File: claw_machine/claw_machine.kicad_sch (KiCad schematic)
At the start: 21 parts, among them J101 Conn_01x04, J102 Conn_01x04, J103 Conn_01x04, J12V_1 Screw_Terminal_01x02, J12V_2 Screw_Terminal_01x02, J5V_1 Screw_Terminal_01x02, J5V_2 Screw_Terminal_01x02, SW4 SW_Push

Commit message: Tiny bit of PCB work
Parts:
- added C101, C102: 100u, Capacitor_THT:CP_Radial_D10.0mm_P5.00mm_P7.50mm, symbol Device:C_Polarized
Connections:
- net +12V: now also C101.1
- net +5V: now also C102.1
- net GND: now also C101.2, C102.2
- no-connect marks 27 -> 33
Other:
- note added: "Motor Bypass Caps"
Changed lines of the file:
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@@
   (no_connect (at 43.18 121.92))
   (no_connect (at 43.18 86.36))
+  (no_connect (at 43.18 35.56))
   (no_connect (at 43.18 83.82))
+  (no_connect (at 43.18 43.18))
   (no_connect (at 80.01 13.97))
   (no_connect (at 77.47 13.97))
   (no_connect (at 109.22 48.26))
+  (no_connect (at 43.18 40.64))
   (no_connect (at 109.22 45.72))
+  (no_connect (at 43.18 38.1))
   (no_connect (at 109.22 132.08))
   (no_connect (at 43.18 76.2))
+  (no_connect (at 43.18 48.26))
   (no_connect (at 43.18 81.28))
   (no_connect (at 109.22 129.54))
@@
   (no_connect (at 43.18 99.06))
   (no_connect (at 109.22 134.62))
+  (no_connect (at 43.18 45.72))
   (no_connect (at 43.18 78.74))
   (no_connect (at 43.18 96.52))
@@
   (no_connect (at 43.18 91.44))
   (no_connect (at 74.93 13.97))
+  (wire (pts (xy 173.99 121.92) (xy 173.99 123.19))
+    (stroke (width 0) (type default))
+  )
   (wire (pts (xy 109.22 109.22) (xy 124.46 109.22))
     (stroke (width 0) (type default))
@@
     (stroke (width 0) (type default))
   )
+  (wire (pts (xy 186.69 121.92) (xy 186.69 123.19))
+    (stroke (width 0) (type default))
+  )
   (wire (pts (xy 39.37 104.14) (xy 43.18 104.14))
     (stroke (width 0) (type default))
   )
+  (wire (pts (xy 173.99 113.03) (xy 173.99 114.3))
+    (stroke (width 0) (type default))
+  )
   (wire (pts (xy 109.22 68.58) (xy 118.11 68.58))
     (stroke (width 0) (type default))
@@
     (stroke (width 0) (type default))
   )
+  (wire (pts (xy 186.69 113.03) (xy 186.69 114.3))
+    (stroke (width 0) (type default))
+  )
   (wire (pts (xy 26.67 193.04) (xy 26.67 191.77))
     (stroke (width 0) (type default))
@@
   )
   (rectangle (start 48.26 154.94) (end 101.6 200.66)
+    (stroke (width 0) (type default))
+    (fill (type none))
+  )
+  (rectangle (start 160.02 106.68) (end 215.9 129.54)
     (stroke (width 0) (type default))
     (fill (type none))
@@
   )
   (text "Stepper Drivers" (at 229.87 109.22 0)
+    (effects (font (size 1.27 1.27) (thickness 0.254) bold) (justify left bottom))
+  )
+  (text "Motor Bypass Caps" (at 195.58 110.49 0)
     (effects (font (size 1.27 1.27) (thickness 0.254) bold) (justify left bottom))
   )
@@
     )
   )
+  (symbol (lib_id "power:+12V") (at 173.99 113.03 0) (unit 1)
+    (in_bom yes) (on_board yes) (dnp no)
+    (property "Reference" "#PWR0121" (at 173.99 116.84 0)
+      (effects (font (size 1.27 1.27)) hide)
+    )
+    (property "Value" "+12V" (at 170.18 109.22 0)
+      (effects (font (size 1.27 1.27)) (justify left))
+    )
+    (property "Footprint" "" (at 173.99 113.03 0)
+      (effects (font (size 1.27 1.27)) hide)
+    )
+    (property "Datasheet" "" (at 173.99 113.03 0)
+      (effects (font (size 1.27 1.27)) hide)
+    )
+    (pin "1")
+    (instances
+      (project "claw_machine"
+        (path "/2e48e9a4-e55f-4bd7-8086-6a8b9c5eabc1"
+          (reference "#PWR0121") (unit 1)
+        )
+      )
+      (project "ClawMachine"
+        (path "/aafe1d38-cfbd-4a85-a256-fbe14cd8b9f5"
+          (reference "#PWR046") (unit 1)
+        )
+      )
+    )
+  )
   (symbol (lib_id "Mechanical:MountingHole") (at 172.72 168.91 0) (unit 1)
     (in_bom yes) (on_board yes) (dnp no) (fields_autoplaced)
@@
     )
   )
+  (symbol (lib_id "power:GND") (at 173.99 123.19 0) (unit 1)
+    (in_bom yes) (on_board yes) (dnp no)
+    (property "Reference" "#PWR0122" (at 173.99 129.54 0)
+      (effects (font (size 1.27 1.27)) hide)
+    )
+    (property "Value" "GND" (at 173.99 127 0)
+      (effects (font (size 1.27 1.27)))
+    )
+    (property "Footprint" "" (at 173.99 123.19 0)
+      (effects (font (size 1.27 1.27)) hide)
+    )
+    (property "Datasheet" "" (at 173.99 123.19 0)
+      (effects (font (size 1.27 1.27)) hide)
+    )
+    (pin "1")
+    (instances
+      (project "claw_machine"
+        (path "/2e48e9a4-e55f-4bd7-8086-6a8b9c5eabc1"
+          (reference "#PWR0122") (unit 1)
+        )
+      )
+    )
+  )
   (symbol (lib_id "Switch:SW_Push") (at 34.29 104.14 0) (unit 1)
     (in_bom yes) (on_board yes) (dnp no)
@@
     )
   )
+  (symbol (lib_id "power:GND") (at 186.69 123.19 0) (unit 1)
+    (in_bom yes) (on_board yes) (dnp no)
+    (property "Reference" "#PWR0125" (at 186.69 129.54 0)
+      (effects (font (size 1.27 1.27)) hide)
+    )
+    (property "Value" "GND" (at 186.69 127 0)
+      (effects (font (size 1.27 1.27)))
+    )
+    (property "Footprint" "" (at 186.69 123.19 0)
+      (effects (font (size 1.27 1.27)) hide)
+    )
+    (property "Datasheet" "" (at 186.69 123.19 0)
+      (effects (font (size 1.27 1.27)) hide)
+    )
+    (pin "1")
+    (instances
+      (project "claw_machine"
+        (path "/2e48e9a4-e55f-4bd7-8086-6a8b9c5eabc1"
+          (reference "#PWR0125") (unit 1)
+        )
+      )
+    )
+  )
   (symbol (lib_id "power:+5V") (at 201.93 158.75 0) (unit 1)
     (in_bom yes) (on_board yes) (dnp no)
@@
     )
   )
+  (symbol (lib_id "Device:C_Polarized") (at 186.69 118.11 0) (unit 1)
+    (in_bom yes) (on_board yes) (dnp no) (fields_autoplaced)
+    (property "Reference" "C102" (at 190.5 115.951 0)
+      (effects (font (size 1.27 1.27)) (justify left))
+    )
+    (property "Value" "100u" (at 190.5 118.491 0)
+      (effects (font (size 1.27 1.27)) (justify left))
+    )
+    (property "Footprint" "Capacitor_THT:CP_Radial_D10.0mm_P5.00mm_P7.50mm" (at 187.6552 121.92 0)
+      (effects (font (size 1.27 1.27)) hide)
+    )
+    (property "Datasheet" "~" (at 186.69 118.11 0)
+      (effects (font (size 1.27 1.27)) hide)
+    )
+    (pin "1")
+    (pin "2")
+    (instances
+      (project "claw_machine"
+        (path "/2e48e9a4-e55f-4bd7-8086-6a8b9c5eabc1"
+          (reference "C102") (unit 1)
+        )
+      )
+    )
+  )
   (symbol (lib_id "Device:LED") (at 69.85 180.34 90) (unit 1)
     (in_bom yes) (on_board yes) (dnp no)
@@
         (path "/aafe1d38-cfbd-4a85-a256-fbe14cd8b9f5"
           (reference "#PWR047") (unit 1)
+        )
+      )
+    )
+  )
+  (symbol (lib_id "power:+5V") (at 186.69 113.03 0) (unit 1)
+    (in_bom yes) (on_board yes) (dnp no)
+    (property "Reference" "#PWR0123" (at 186.69 116.84 0)
+      (effects (font (size 1.27 1.27)) hide)
+    )
+    (property "Value" "+5V" (at 186.69 109.22 0)
+      (effects (font (size 1.27 1.27)))
+    )
+    (property "Footprint" "" (at 186.69 113.03 0)
+      (effects (font (size 1.27 1.27)) hide)
+    )
+    (property "Datasheet" "" (at 186.69 113.03 0)
+      (effects (font (size 1.27 1.27)) hide)
+    )
+    (pin "1")
+    (instances
+      (project "claw_machine"
+        (path "/2e48e9a4-e55f-4bd7-8086-6a8b9c5eabc1"
+          (reference "#PWR0123") (unit 1)
         )
       )
@@
     )
   )
+  (symbol (lib_id "Device:C_Polarized") (at 173.99 118.11 0) (unit 1)
+    (in_bom yes) (on_board yes) (dnp no) (fields_autoplaced)
+    (property "Reference" "C101" (at 177.8 115.951 0)
+      (effects (font (size 1.27 1.27)) (justify left))
+    )
+    (property "Value" "100u" (at 177.8 118.491 0)
+      (effects (font (size 1.27 1.27)) (justify left))
+    )
+    (property "Footprint" "Capacitor_THT:CP_Radial_D10.0mm_P5.00mm_P7.50mm" (at 174.9552 121.92 0)
+      (effects (font (size 1.27 1.27)) hide)
+    )
+    (property "Datasheet" "~" (at 173.99 118.11 0)
+      (effects (font (size 1.27 1.27)) hide)
+    )
+    (pin "1")
+    (pin "2")
+    (instances
+      (project "claw_machine"
+        (path "/2e48e9a4-e55f-4bd7-8086-6a8b9c5eabc1"
+          (reference "C101") (unit 1)
+        )
+      )
+    )
+  )
   (symbol (lib_id "Connector:Screw_Terminal_01x02") (at 208.28 161.29 0) (unit 1)
     (in_bom yes) (on_board yes) (dnp yes) (fields_autoplaced)
@@
       )
       (project "claw_machine"
-        (path "/2e48e9a4-e55f-4bd7-8086-6a8b9c5eabc1" (page "6"))
+        (path "/2e48e9a4-e55f-4bd7-8086-6a8b9c5eabc1" (page "4"))
       )
     )
@@
       )
       (project "claw_machine"
-        (path "/2e48e9a4-e55f-4bd7-8086-6a8b9c5eabc1" (page "4"))
-      )
-    )
+        (path "/2e48e9a4-e55f-4bd7-8086-6a8b9c5eabc1" (page "6"))
+      )
+    )

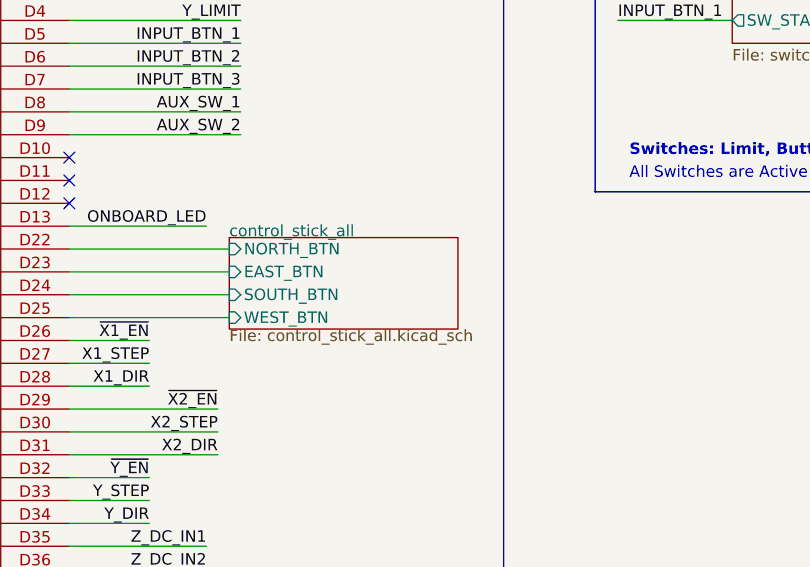
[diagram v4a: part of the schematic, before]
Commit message: Do most of the PCB layout
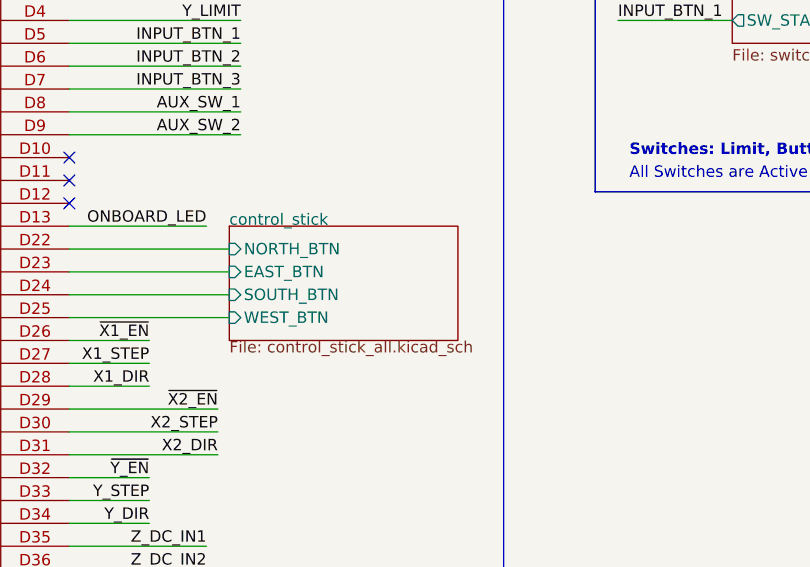
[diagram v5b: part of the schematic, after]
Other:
- sheet control_stick_all renamed control_stick
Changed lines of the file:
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@@
     )
   )
-  (sheet (at 127 54.61) (size 25.4 10.16)
+  (sheet (at 127 53.34) (size 25.4 12.7)
     (stroke (width 0.1524) (type solid))
     (fill (color 0 0 0 0.0000))
-    (property "Sheetname" "control_stick_all" (at 127 54.61 0)
+    (property "Sheetname" "control_stick" (at 127 53.34 0)
       (effects (font (size 1.27 1.27)) (justify left bottom))
     )
-    (property "Sheetfile" "control_stick_all.kicad_sch" (at 127 64.77 0)
+    (property "Sheetfile" "control_stick_all.kicad_sch" (at 127 66.04 0)
       (effects (font (size 1.27 1.27)) (justify left top))
     )

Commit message: Tweaks
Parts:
- H101, H102, H103, H104: footprint MountingHole:MountingHole_4mm -> MountingHole:MountingHole_4.3mm_M4_Pad_TopBottom; symbol Mechanical:MountingHole -> Mechanical:MountingHole_Pad
- J101: value Conn_01x04 -> ~; footprint Connector_PinHeader_2.54mm:PinHeader_1x04_P2.54mm_Vertical -> Connector_PinHeader_2.54mm:PinHeader_2x04_P2.54mm_Vertical; symbol Connector_Generic:Conn_01x04 -> Connector_Generic:Conn_02x04_Odd_Even
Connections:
- net +5V: now also J101.2 (Pin_2)
- net GND: now also J101.7 (Pin_7), J101.8 (Pin_8); no longer J101.4 (Pin_4)
- net I2C_SCL: now also J101.5 (Pin_5), J101.6 (Pin_6); no longer J101.3 (Pin_3)
- net I2C_SDA: now also J101.3 (Pin_3), J101.4 (Pin_4); no longer J101.2 (Pin_2)
- no-connect marks 33 -> 37
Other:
- moved on the sheet: LED_12V_101, LED_5V_101, LED_OB_101, R101, R102, R103, R104, R105

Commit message: Finish, Gerbers
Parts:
- added J104: Conn_02x06_Odd_Even, Connector_PinHeader_2.54mm:PinHeader_2x06_P2.54mm_Vertical, symbol Connector_Generic:Conn_02x06_Odd_Even
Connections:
- net +5V: now also J104.10 (Pin_10), J104.9 (Pin_9)
- net GND: now also J104.3 (Pin_3), J104.4 (Pin_4)
- net Z_ENC_SIG_1: now reaches A101.D51 (D51_MOSI)
- net Z_ENC_SIG_1: now also J104.5 (Pin_5), J104.6 (Pin_6)
- net Z_ENC_SIG_2: now reaches A101.D52 (D52_SCK)
- net Z_ENC_SIG_2: now also J104.7 (Pin_7), J104.8 (Pin_8)
- new net Z_OUT1: J104.1 (Pin_1), J104.2 (Pin_2)
- new net Z_OUT2: J104.11 (Pin_11), J104.12 (Pin_12)
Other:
- removed sheet dc_driver_claw
- sheet dc_driver_z ports: added  OUT1,  OUT2,  OUT3,  OUT4; removed none
- note added: "Order on Motor: Red[1] (MTR +/OUT1) Black (ENC -) Yellow (SIG 1) Green (SIG 2) Blue (ENC +) White (MTR -/OUT2)"
- note added: "Z Motor Connector (Drive and Encoder)"

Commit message: Update schematic text, remove unused nets for CLAW motor
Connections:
- net CLAW_DC_EN_A: no longer names the net of A101.D45
- net CLAW_DC_EN_B: no longer names the net of A101.D46
- net CLAW_DC_IN1: no longer names the net of A101.D41
- net CLAW_DC_IN2: no longer names the net of A101.D42
- net CLAW_DC_IN3: no longer names the net of A101.D43
- net CLAW_DC_IN4: no longer names the net of A101.D44
- no-connect marks 37 -> 43
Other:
- note added: "OUT3 and OUT4 are only on subpage terminal block"
- note added: "Rev1 marked these pins as CLAW_XXX"
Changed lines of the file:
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@@
 (kicad_sch (version 20230121) (generator eeschema)
   (paper "USLetter")
+  (title_block
+    (rev "1")
+  )
   (junction (at 36.83 186.69) (diameter 0) (color 0 0 0 0)
   )
@@
   (no_connect (at 43.18 86.36))
   (no_connect (at 43.18 35.56))
+  (no_connect (at 109.22 116.84))
   (no_connect (at 162.56 161.29))
   (no_connect (at 43.18 83.82))
+  (no_connect (at 109.22 106.68))
   (no_connect (at 43.18 43.18))
   (no_connect (at 80.01 13.97))
@@
   (no_connect (at 43.18 40.64))
   (no_connect (at 109.22 45.72))
+  (no_connect (at 109.22 104.14))
   (no_connect (at 43.18 38.1))
   (no_connect (at 43.18 76.2))
   (no_connect (at 43.18 48.26))
   (no_connect (at 43.18 81.28))
+  (no_connect (at 109.22 114.3))
+  (no_connect (at 109.22 109.22))
   (no_connect (at 256.54 135.89))
   (no_connect (at 109.22 50.8))
@@
   (no_connect (at 43.18 71.12))
   (no_connect (at 43.18 88.9))
+  (no_connect (at 109.22 111.76))
   (no_connect (at 82.55 13.97))
   (no_connect (at 43.18 106.68))
@@
     (stroke (width 0) (type default))
   )
-  (wire (pts (xy 109.22 109.22) (xy 124.46 109.22))
-    (stroke (width 0) (type default))
-  )
   (wire (pts (xy 40.64 25.4) (xy 43.18 25.4))
     (stroke (width 0) (type default))
@@
     (stroke (width 0) (type default))
   )
-  (wire (pts (xy 109.22 114.3) (xy 124.46 114.3))
-    (stroke (width 0) (type default))
-  )
   (wire (pts (xy 109.22 66.04) (xy 118.11 66.04))
     (stroke (width 0) (type default))
@@
     (stroke (width 0) (type default))
   )
-  (wire (pts (xy 109.22 116.84) (xy 124.46 116.84))
-    (stroke (width 0) (type default))
-  )
   (wire (pts (xy 36.83 168.91) (xy 36.83 186.69))
     (stroke (width 0) (type default))
@@
     (stroke (width 0) (type default))
   )
-  (wire (pts (xy 109.22 111.76) (xy 124.46 111.76))
-    (stroke (width 0) (type default))
-  )
   (wire (pts (xy 204.47 20.32) (xy 213.36 20.32))
     (stroke (width 0) (type default))
   )
-  (wire (pts (xy 109.22 104.14) (xy 124.46 104.14))
-    (stroke (width 0) (type default))
-  )
   (wire (pts (xy 40.64 33.02) (xy 43.18 33.02))
     (stroke (width 0) (type default))
@@
     (stroke (width 0) (type default))
   )
-  (wire (pts (xy 109.22 106.68) (xy 124.46 106.68))
-    (stroke (width 0) (type default))
-  )
   (wire (pts (xy 109.22 101.6) (xy 124.46 101.6))
     (stroke (width 0) (type default))
@@
   (text "Stepper Drivers" (at 229.87 109.22 0)
     (effects (font (size 1.27 1.27) (thickness 0.254) bold) (justify left bottom))
+  )
+  (text "Rev1 marked these\n  pins as CLAW_XXX" (at 111.76 110.49 0)
+    (effects (font (size 1.27 1.27)) (justify left bottom))
+  )
+  (text "OUT3 and OUT4 are\n  only on subpage\n  terminal block"
+    (at 245.11 151.13 0)
+    (effects (font (size 1.27 1.27)) (justify left bottom))
   )
   (text "Order on Motor:\nRed[1] (MTR +/OUT1)\nBlack (ENC -)\nYellow (SIG 1)\nGreen (SIG 2)\nBlue (ENC +)\nWhite (MTR -/OUT2)"
@@
     (effects (font (size 1.27 1.27)) (justify right bottom))
   )
-  (label "Z_ENC_SIG_2" (at 125.73 132.08 0) (fields_autoplaced)
-    (effects (font (size 1.27 1.27)) (justify left bottom))
+  (label "Z_ENC_SIG_2" (at 125.73 132.08 180) (fields_autoplaced)
+    (effects (font (size 1.27 1.27)) (justify right bottom))
   )
   (label "Z_ENC_SIG_2" (at 187.96 93.98 0) (fields_autoplaced)
     (effects (font (size 1.27 1.27)) (justify left bottom))
   )
-  (label "Z_ENC_SIG_1" (at 125.73 129.54 0) (fields_autoplaced)
-    (effects (font (size 1.27 1.27)) (justify left bottom))
+  (label "Z_ENC_SIG_1" (at 125.73 129.54 180) (fields_autoplaced)
+    (effects (font (size 1.27 1.27)) (justify right bottom))
   )
   (label "Y_LIMIT" (at 236.22 20.32 0) (fields_autoplaced)
@@
     (effects (font (size 1.27 1.27)) (justify right bottom))
   )
-  (label "CLAW_DC_IN2" (at 124.46 106.68 180) (fields_autoplaced)
-    (effects (font (size 1.27 1.27)) (justify right bottom))
-  )
   (label "Z_DC_EN_B" (at 226.06 140.97 0) (fields_autoplaced)
     (effects (font (size 1.27 1.27)) (justify left bottom))
@@
     (effects (font (size 1.27 1.27)) (justify left bottom))
   )
-  (label "CLAW_DC_EN_B" (at 124.46 116.84 180) (fields_autoplaced)
-    (effects (font (size 1.27 1.27)) (justify right bottom))
-  )
   (label "X2_DIR" (at 226.06 83.82 0) (fields_autoplaced)
     (effects (font (size 1.27 1.27)) (justify left bottom))
@@
     (effects (font (size 1.27 1.27)) (justify right bottom))
   )
-  (label "CLAW_DC_IN3" (at 124.46 109.22 180) (fields_autoplaced)
-    (effects (font (size 1.27 1.27)) (justify right bottom))
-  )
   (label "INPUT_BTN_2" (at 200.66 31.75 0) (fields_autoplaced)
     (effects (font (size 1.27 1.27)) (justify left bottom))
@@
     (effects (font (size 1.27 1.27)) (justify right bottom))
   )
-  (label "CLAW_DC_IN4" (at 124.46 111.76 180) (fields_autoplaced)
-    (effects (font (size 1.27 1.27)) (justify right bottom))
-  )
   (label "X2_LIMIT" (at 204.47 20.32 0) (fields_autoplaced)
     (effects (font (size 1.27 1.27)) (justify left bottom))
   )
-  (label "CLAW_DC_IN1" (at 124.46 104.14 180) (fields_autoplaced)
-    (effects (font (size 1.27 1.27)) (justify right bottom))
-  )
-  (label "CLAW_DC_EN_A" (at 124.46 114.3 180) (fields_autoplaced)
-    (effects (font (size 1.27 1.27)) (justify right bottom))
-  )
   (label "X1_LIMIT" (at 173.99 20.32 0) (fields_autoplaced)
